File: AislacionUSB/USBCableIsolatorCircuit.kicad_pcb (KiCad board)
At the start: 2 copper layers, 57.4 x 45 mm, 63 parts, among them CON1 BARREL_JACK, J1 MICRO_USB, J2 IN_VCC, P1 USB_A, U1 PRTR5V0U2X, U2 ADUM5000, U3 7805, U4 PRTR5V0U2X, U5 ADUM4160

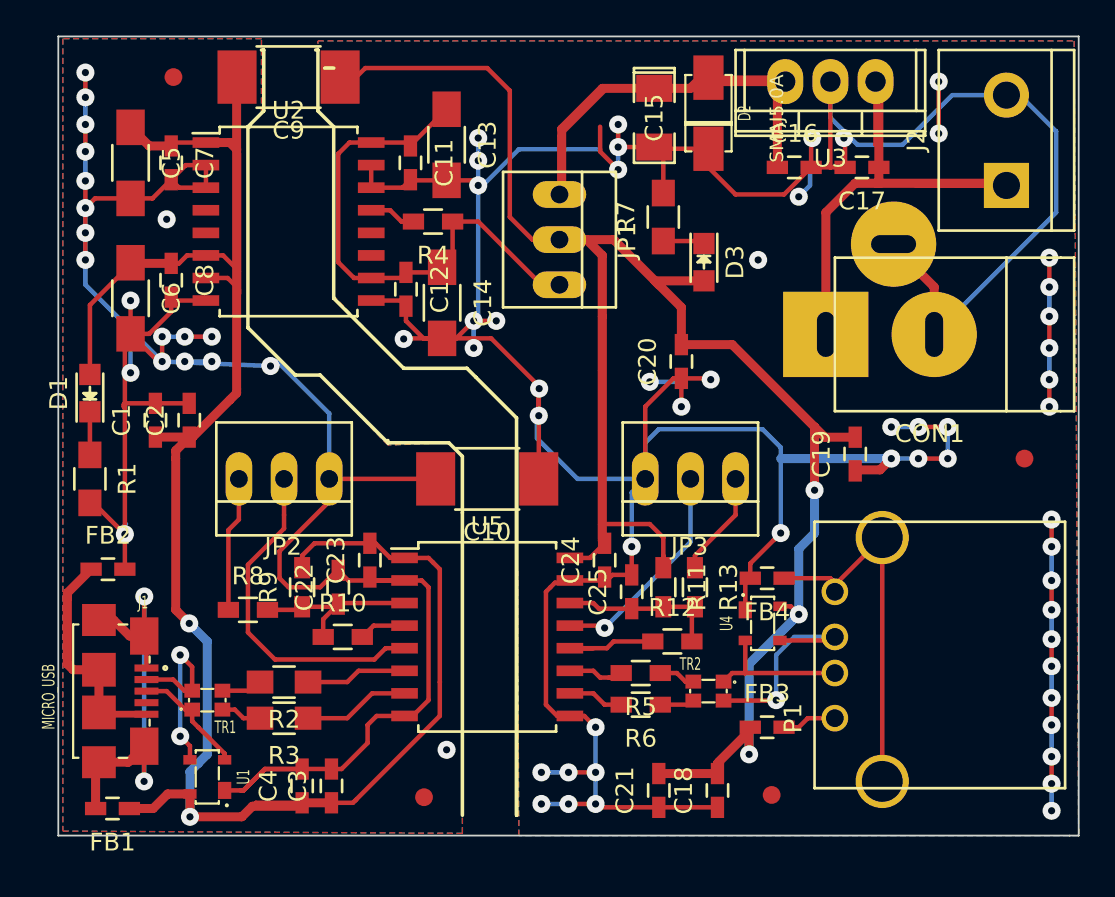
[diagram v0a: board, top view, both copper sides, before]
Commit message: Leyendas en el PCB
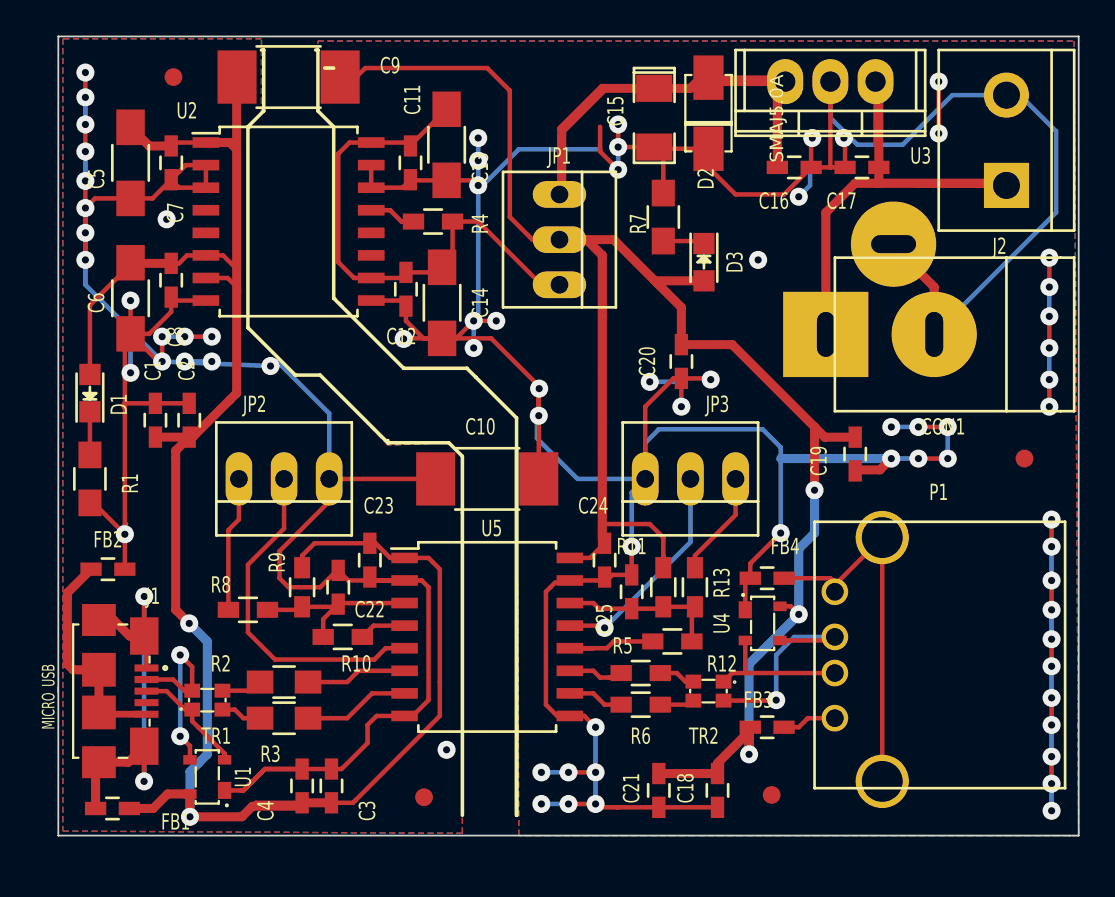
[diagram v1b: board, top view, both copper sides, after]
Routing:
- net (no net): track 1.52 -> 34.3 mm, vias 3 -> 27
- net GNDA: track 252.7 -> 221.6 mm, vias 53 -> 31
- net GND: track 132.6 -> 130.9 mm, vias 17 -> 15

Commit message: Se agregaron cambios sugeridos por el docente - DOC:Sugerencias Docente 20160724
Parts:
- added H1: PCB_HOLE, Mounting_Holes:MountingHole_2.7mm_M2.5_DIN965_Pad, F.Cu at (123.3, 96.9)
- added H2: PCB_HOLE, Mounting_Holes:MountingHole_2.7mm_M2.5_DIN965_Pad, F.Cu at (139.2, 117.9)
- added H3: PCB_HOLE, Mounting_Holes:MountingHole_2.7mm_M2.5_DIN965_Pad, F.Cu at (159.0, 99.6)
- C1, C11, C12, C16, C17, C18, C19, C2, C20, C21, C22, C23, C24, C25, C3, C4, C7, C8, FB1, FB2, FB3, FB4: footprint Capacitors_SMD:C_0603_HandSoldering -> AislacionUSB:C_0603_HandSoldering
- C10, C9: footprint Capacitors_SMD:C_1812_HandSoldering -> AislacionUSB:C_1812_HandSoldering
- C13, C14, C5, C6: footprint Capacitors_SMD:C_1206_HandSoldering -> AislacionUSB:C_1206_HandSoldering
- C15: footprint SMD_Packages:SMD-1206_Pol -> AislacionUSB:SMD-1206_Pol
- CON1: footprint Connect:JACK_ALIM -> AislacionUSB:JACK_ALIM
- D1, D3: footprint LEDs:LED_0805 -> AislacionUSB:LED_0805
- J2: footprint Connect:bornier2 -> AislacionUSB:bornier2
- JP1, JP2, JP3: footprint Connect:PINHEAD1-3 -> AislacionUSB:PIN_ARRAY_3x1
- P1: footprint Connect:USB_A -> AislacionUSB:USB_A
- R1, R2, R3, R7: footprint Resistors_SMD:R_0805_HandSoldering -> AislacionUSB:R_0603_HandSoldering
- R10, R11, R12, R13, R4, R5, R6, R8, R9: footprint Resistors_SMD:R_0603_HandSoldering -> AislacionUSB:R_0603_HandSoldering
- U2: footprint Housings_SOIC:SOIC-16_7.5x10.3mm_Pitch1.27mm -> AislacionUSB:ADUM5000
- U3: footprint Power_Integrations:TO-220 -> AislacionUSB:TO-220
- U5: footprint Housings_SOIC:SOIC-16_7.5x10.3mm_Pitch1.27mm -> AislacionUSB:ADUM4160
- moved D2 75.9 mm to (146.9, 80.5)
- moved U4 75.7 mm to (150.1, 109.1)
- moved C1 75.7 mm to (116.0, 97.5)
- moved C11 75.7 mm to (130.3, 83.1)
- moved C12 75.7 mm to (130.0, 90.2)
- moved C15 75.7 mm to (144.0, 80.5)
- moved C16 75.7 mm to (151.9, 83.3)
- moved C17 75.7 mm to (155.7, 83.3)
- moved C19 75.7 mm to (155.3, 99.4)
- moved C2 75.7 mm to (117.9, 97.5)
- moved C20 75.7 mm to (145.5, 94.2)
- moved C21 75.7 mm to (144.3, 118.4)
- moved C22 75.7 mm to (126.2, 106.9)
- moved C23 75.7 mm to (128.0, 105.4)
- moved C24 75.7 mm to (141.2, 105.4)
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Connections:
- F1 pad 1: Net-(F1-Pad1) -> (no net)
- F2 pad 1: Net-(F2-Pad1) -> (no net)
- F3 pad 1: Net-(F3-Pad1) -> (no net)
- F4 pad 1: Net-(F4-Pad1) -> (no net)
- J1 pad 4: Net-(J1-Pad4) -> (no net)
- U2 pad 11: Net-(U2-Pad11) -> (no net)
- U2 pad 12: Net-(U2-Pad12) -> (no net)
- U2 pad 4: Net-(U2-Pad4) -> (no net)
- U2 pad 5: Net-(U2-Pad5) -> (no net)
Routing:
- net +5V_iso: track 153.8 -> 123.9 mm
- net (no net): track 34.3 -> 6.60 mm, vias 27 -> 0
- net Net-(C17-Pad1): track 51.4 -> 26.4 mm
- net GNDA: track 221.6 -> 243.6 mm, vias 31 -> 17
- net Net-(C15-Pad1): track 40.7 -> 24.4 mm
- net +5V: track 140.4 -> 127.8 mm, vias 2 -> 4
- net GND: track 130.9 -> 137.3 mm, vias 15 -> 14
- net Net-(P1-Pad2): track 8.33 -> 11.4 mm
- net Net-(D1-Pad1): track 2.43 -> 5.10 mm
- net Net-(J1-Pad2): track 11.2 -> 13.7 mm
- net /ADUM4160/UD+: track 6.01 -> 8.46 mm
- net /ADUM4160/UD-: track 5.69 -> 8.02 mm
- net Net-(FB1-Pad2): track 31.6 -> 33.1 mm
- net Net-(J1-Pad3): track 6.58 -> 7.98 mm
- net Net-(C22-Pad1): track 10.1 -> 11.3 mm
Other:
- net class Default: trace_width 0.254 -> 0.3048
- net class USB added: clearance 0.2032, trace_width 0.254, via_dia 1.016, via_drill 0.4
- board text added: "AuslacionUSB"
- board text added: "REV00"

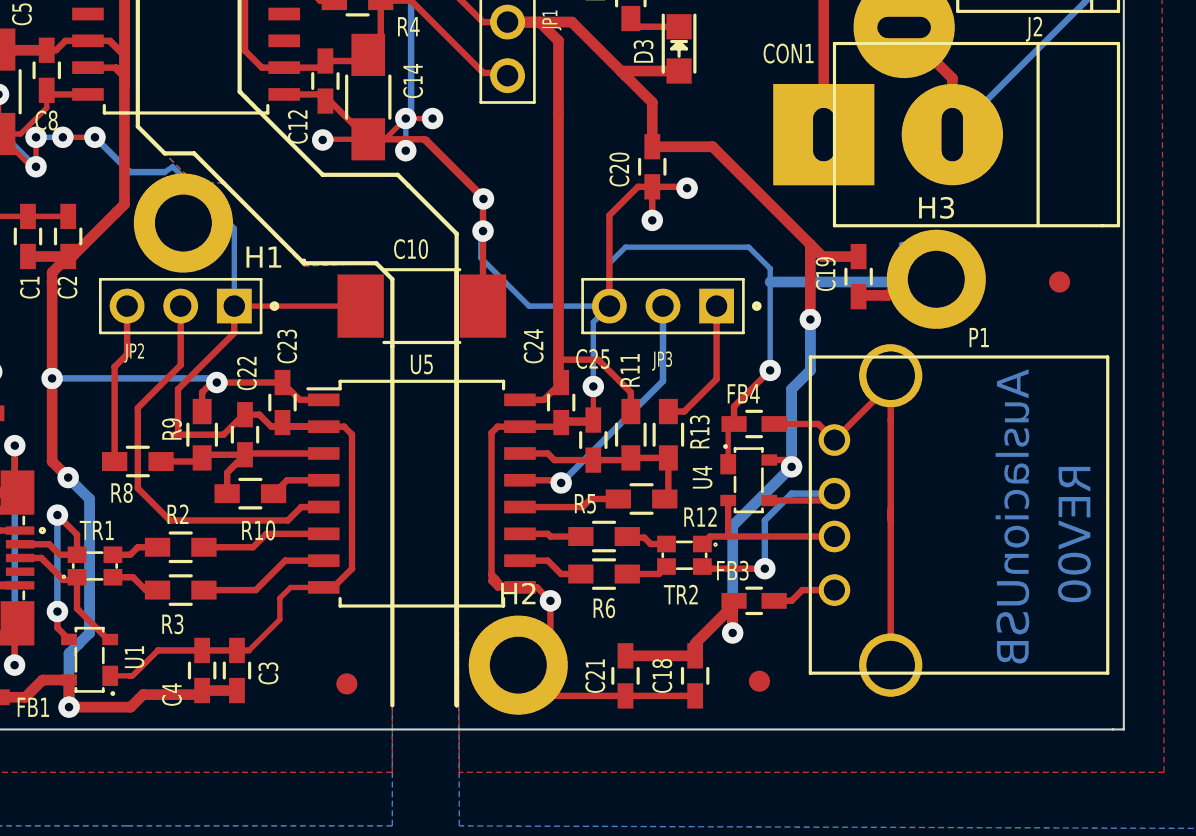
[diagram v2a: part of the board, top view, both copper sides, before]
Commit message: Logo en el PCB - Datos del PCB
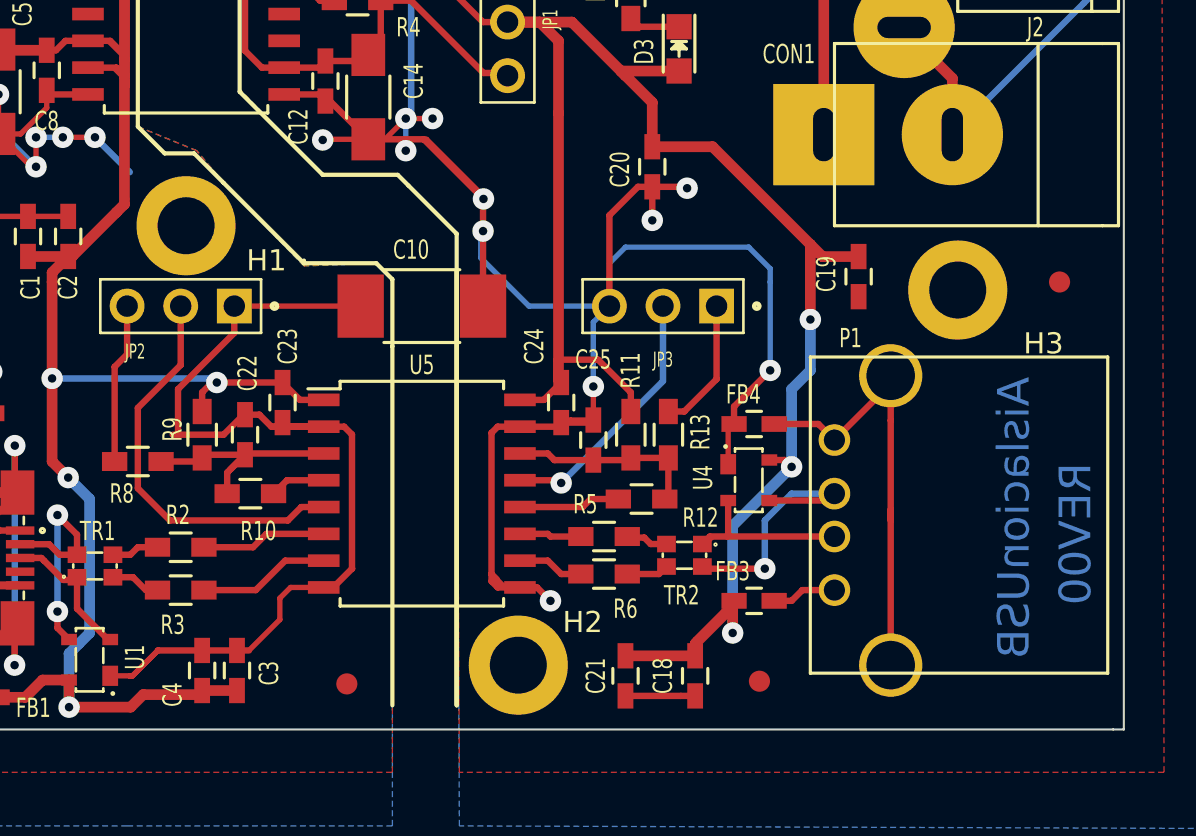
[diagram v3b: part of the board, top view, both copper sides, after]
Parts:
- added OPEN HARDWARE: OSHWA, AislacionUSB:OSHWA, B.Cu at (147.3, 109.2)
- moved H3 1.14 mm to (160.0, 100.1)
- moved H1 0.18 mm to (123.4, 97.0)
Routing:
- net GNDA: track 243.6 -> 216.2 mm
- net GND: track 137.3 -> 127.3 mm
- net (no net): track 6.60 -> 0.00 mm
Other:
- board text added: "AislacionUSB"
- board text added: "CESE - Aislacion USB Diseño de Circuitos Impresos Marcos Darino - REV00"
- board text added: "Material = FR4 Layer = 2 (pth) Thickness = 1.6mm Cooper Thickness = 1 Oz Finish = HASL Solder resist-mask printed (Top & Bottom) Component mask printed (Top & Bottom)"
- board text removed: "AuslacionUSB"

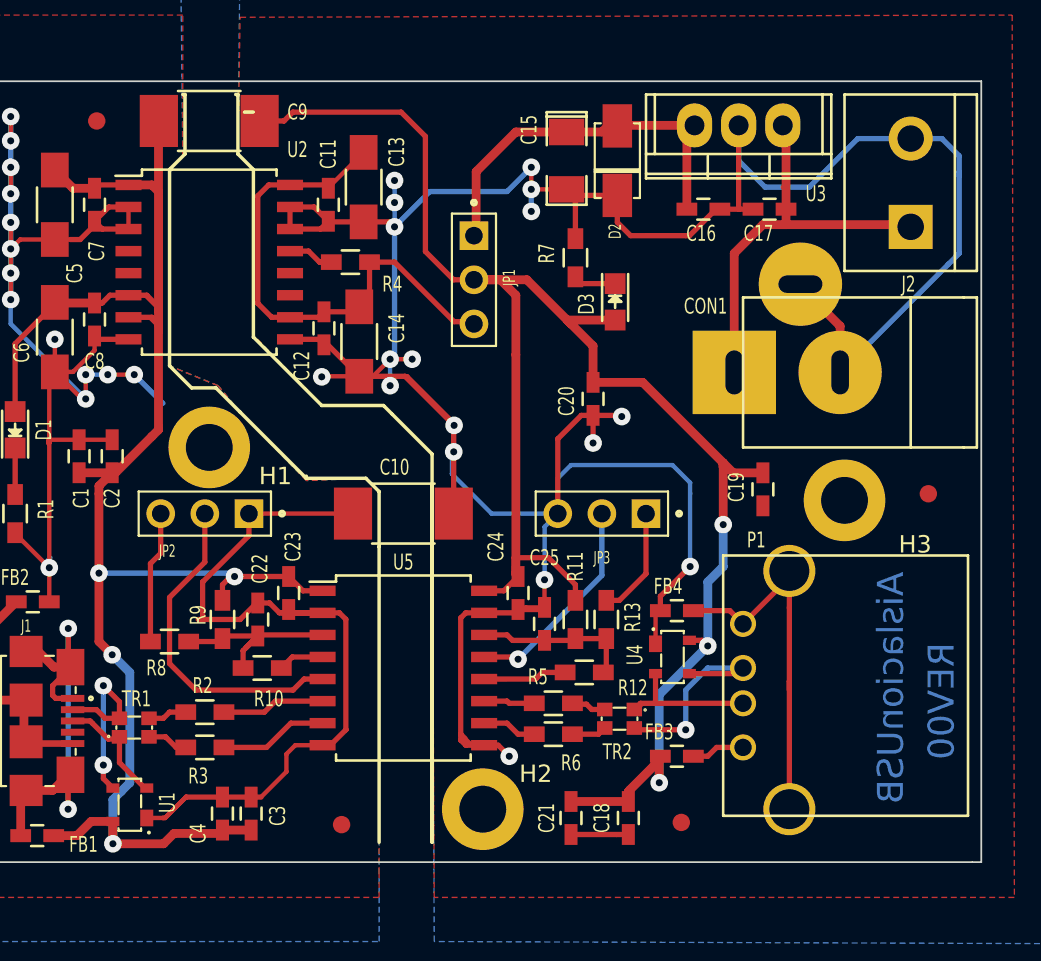
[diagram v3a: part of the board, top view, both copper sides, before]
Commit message: Se agregaron los cambios sugueridos en el doc Aislacion USB - Revision PCB  20160725
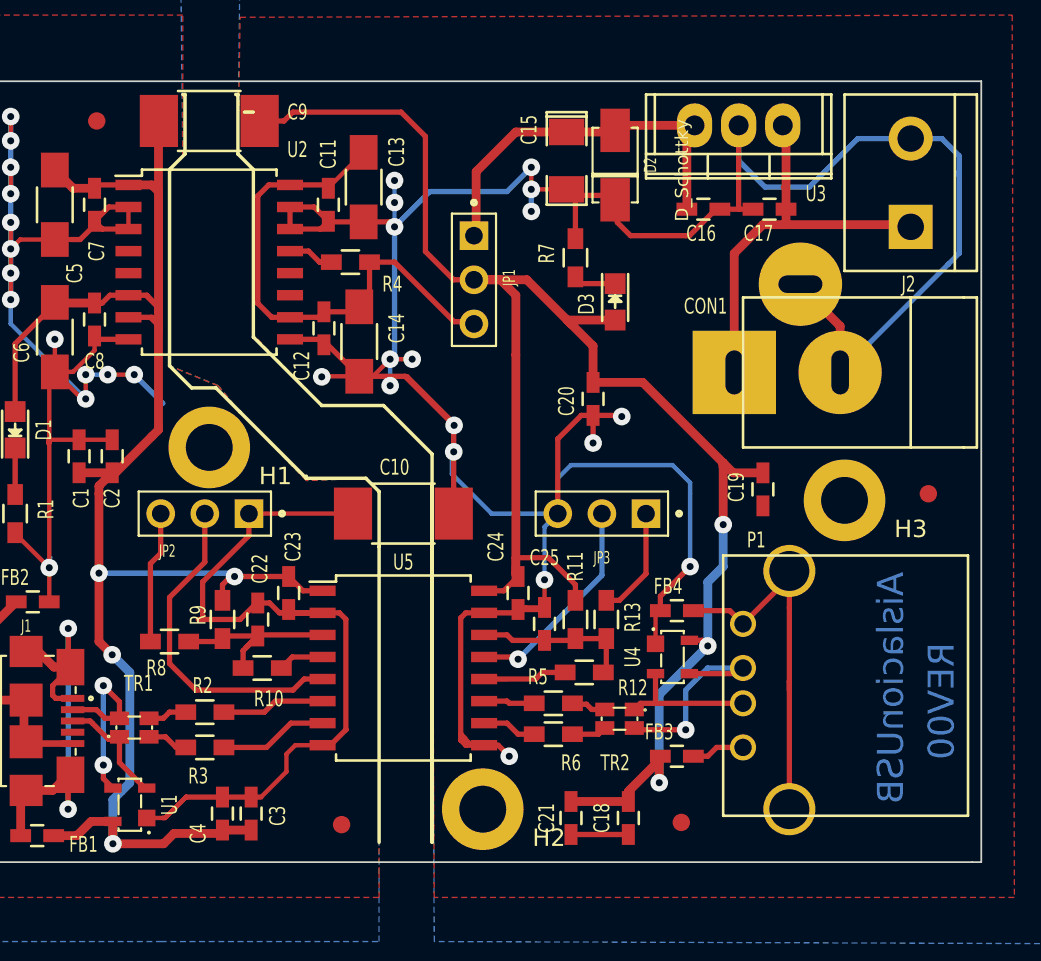
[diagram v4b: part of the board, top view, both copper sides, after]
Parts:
- D2: value SMAJ5.0A -> D_Schottky
- H1, H2, H3: footprint Mounting_Holes:MountingHole_2.7mm_M2.5_DIN965_Pad -> AislacionUSB:MountingHole_2.7mm_M2.5_DIN965_Pad
- TR1, TR2: footprint AislacionUSB:SRF2012 -> AislacionUSB:SRF2012-HandSoldering
- U1, U4: footprint AislacionUSB:SOT-143-4 -> AislacionUSB:SOT-143-4-HandSoldering
- moved D2 0.28 mm to (146.8, 80.8)
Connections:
- F1 pad 1: (no net) -> Net-(F1-Pad1)
- F2 pad 1: (no net) -> Net-(F2-Pad1)
- F3 pad 1: (no net) -> Net-(F3-Pad1)
- F4 pad 1: (no net) -> Net-(F4-Pad1)
- H1 pad 1: (no net) -> GND
- H2 pad 1: (no net) -> GNDA
- H3 pad 1: (no net) -> GNDA
- J1 pad 4: (no net) -> Net-(J1-Pad4)
- U2 pad 11: (no net) -> Net-(U2-Pad11)
- U2 pad 12: (no net) -> Net-(U2-Pad12)
- U2 pad 4: (no net) -> Net-(U2-Pad4)
- U2 pad 5: (no net) -> Net-(U2-Pad5)

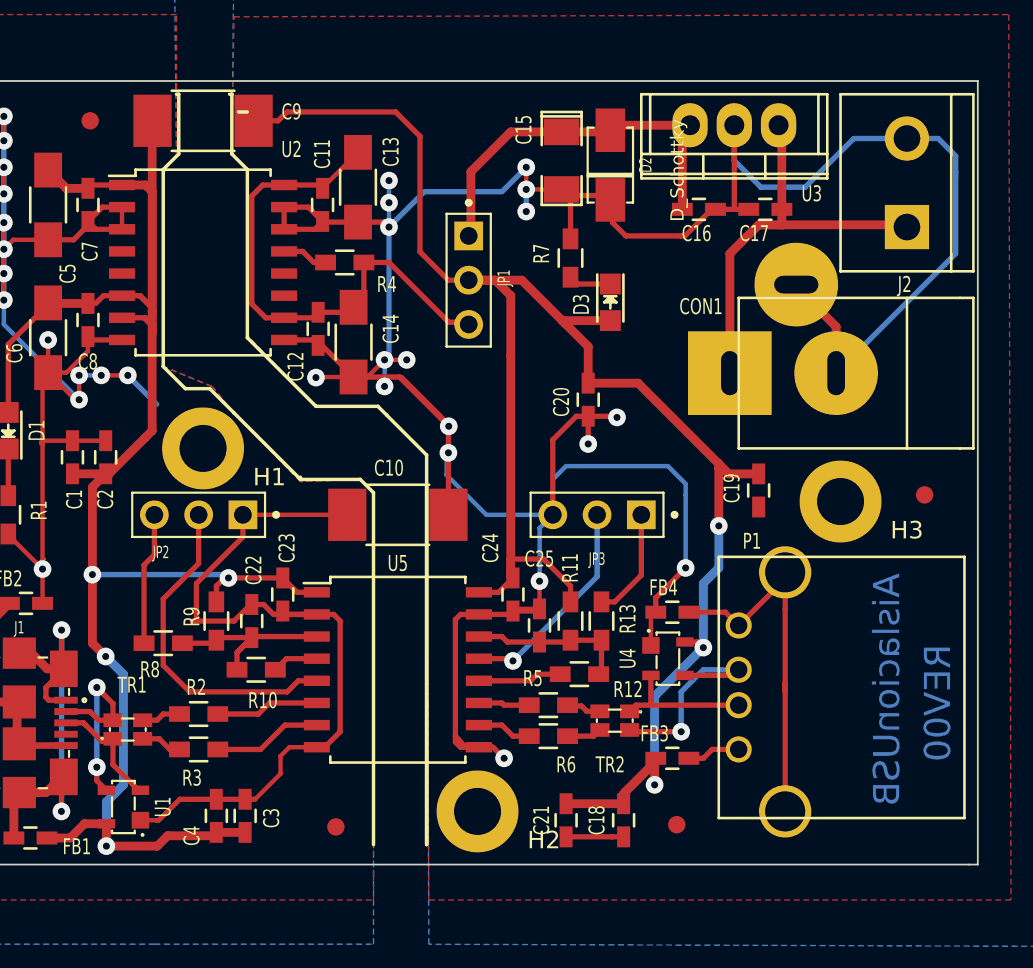
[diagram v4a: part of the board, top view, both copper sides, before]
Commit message: Detalles en la Serigrafia - Se agrego la licencia
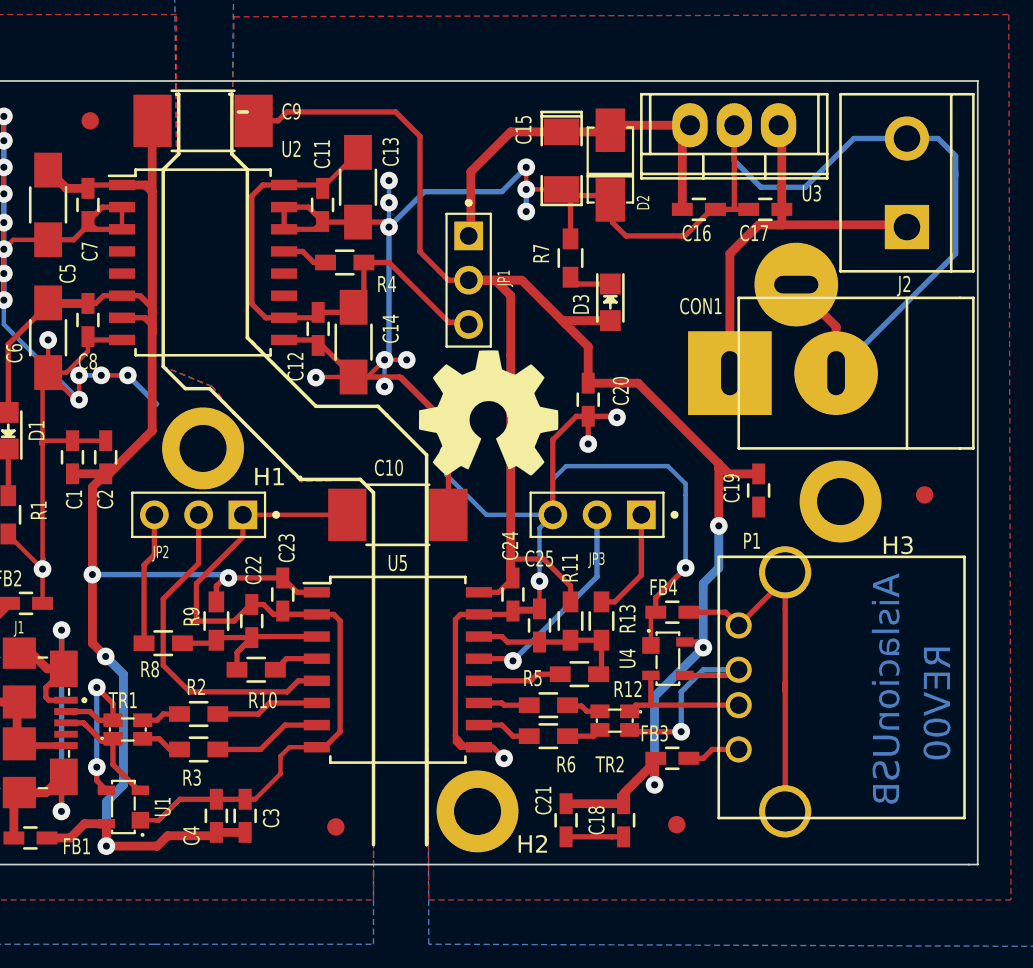
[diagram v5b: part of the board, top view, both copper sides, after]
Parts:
- D2: value D_Schottky -> (none)
- OPEN HARDWARE: moved to F.Cu
- moved OPEN HARDWARE 16.1 mm to (139.8, 95.0), turned to 0 degrees
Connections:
- H1 pad 1: GND -> (no net)
- H2 pad 1: GNDA -> (no net)
- H3 pad 1: GNDA -> (no net)
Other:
- net class USB removed
